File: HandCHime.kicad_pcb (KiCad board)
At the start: 4 copper layers, 38.1 x 22.6 mm, 18 parts, among them J1 USB_C_Receptacle_USB2.0, J2 Pins, SW0 BOOT, SW1 Row 0, Col 0, SW2 Row 0, Col 1, U1 CH552T, U2 USBLC6-2P6

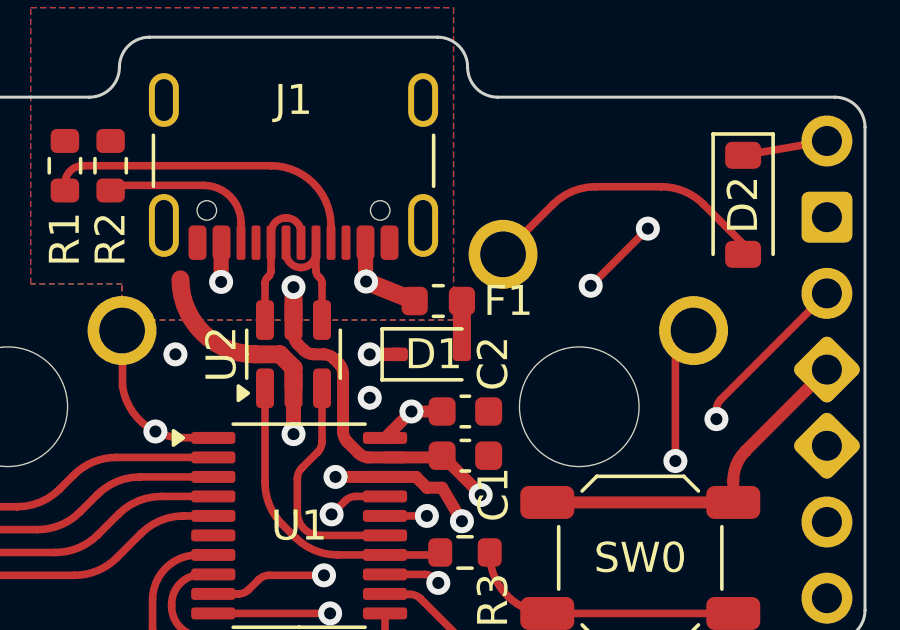
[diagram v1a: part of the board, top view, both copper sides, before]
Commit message: Move fuse away from newly lowered switch
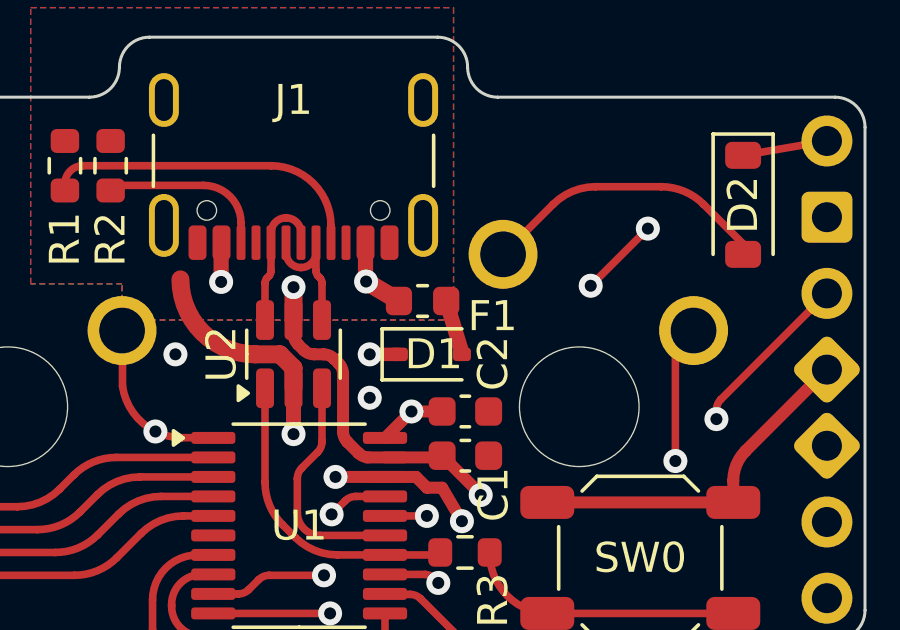
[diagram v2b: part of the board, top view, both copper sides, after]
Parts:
- moved F1 0.53 mm to (163.1, 46.5)
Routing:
- net Net-(D1-A): track 1.27 -> 1.80 mm
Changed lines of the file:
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@@
 	(footprint "Fuse:Fuse_0603_1608Metric"
 		(layer "F.Cu")
-		(at 163.576 46.482)
+		(at 163.051 46.482)
 		(descr "Fuse SMD 0603 (1608 Metric), square (rectangular) end terminal, IPC_7351 nominal, (Body size source: http://www.tortai-tech.com/upload/download/2011102023233369053.pdf), generated with kicad-footprint-generator")
 		(tags "fuse")
 		(property "Reference" "F1"
-			(at 2.3368 0 0)
+			(at 2.3368 0.508 0)
 			(layer "F.SilkS")
 			(effects
@@
 		(fp_arc
 			(start 6.497236 -6.998884)
-			(mid 6.850796 -6.85243)
+			(mid 6.85076 -6.852424)
 			(end 6.997236 -6.498884)
 			(stroke
@@
 		(fp_arc
 			(start 6.497236 -6.998884)
-			(mid 6.850796 -6.85243)
+			(mid 6.85076 -6.852424)
 			(end 6.997236 -6.498884)
 			(stroke
@@
 	)
 	(segment
-		(start 164.3635 48.1)
-		(end 164.3635 46.83)
-		(width 0.6)
+		(start 163.8385 46.482)
+		(end 164.3635 48.2)
+		(width 0.5)
 		(layer "F.Cu")
 		(net 3)
 	)
 	(segment
-		(start 156.337 45.847)
-		(end 156.337 44.805)
-		(width 0.508)
+		(start 161.168965 45.833058)
+		(end 162.2635 46.482)
+		(width 0.6)
 		(layer "F.Cu")
 		(net 4)
 	)
 	(segment
-		(start 161.15 45.814093)
-		(end 161.168965 45.833058)
+		(start 156.337 45.847)
+		(end 156.337 44.805)
 		(width 0.508)
 		(layer "F.Cu")
@@
 	)
 	(segment
-		(start 162.7885 46.482)
+		(start 161.15 45.814093)
 		(end 161.168965 45.833058)
-		(width 0.6)
+		(width 0.508)
 		(layer "F.Cu")
 		(net 4)

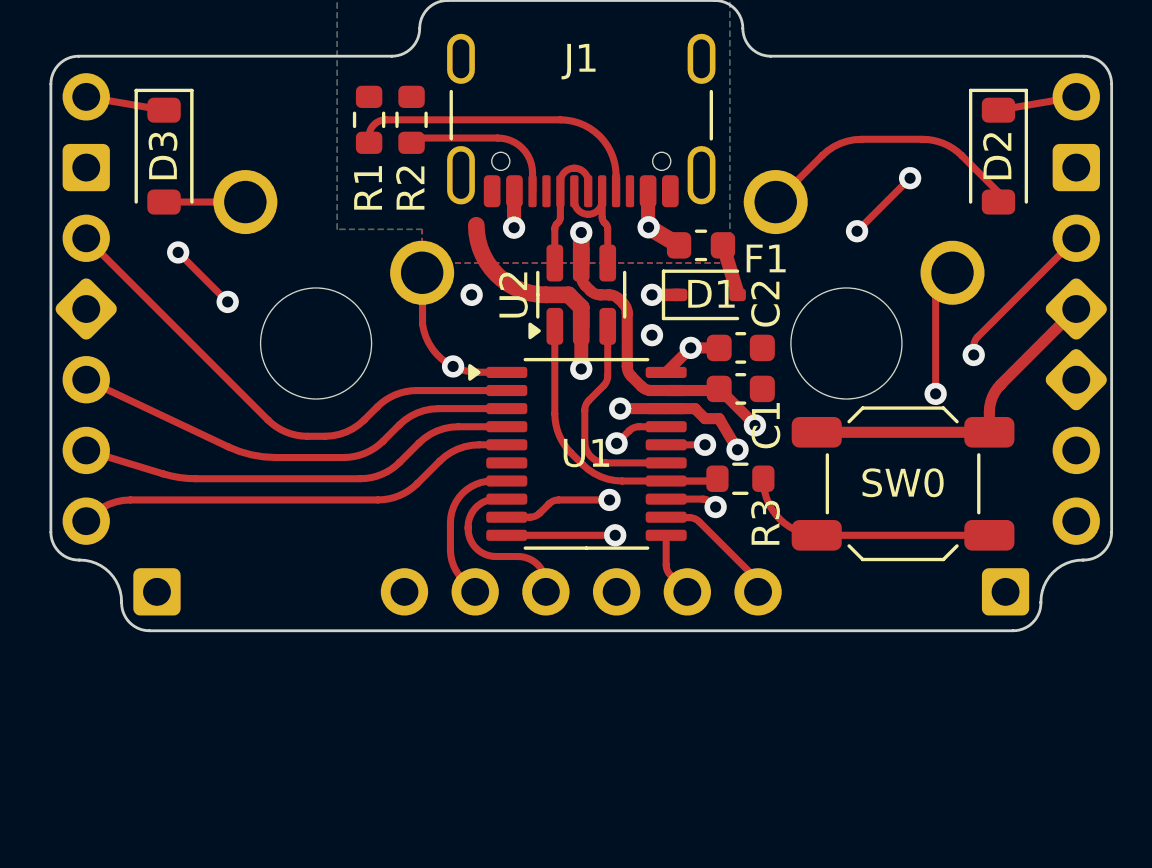
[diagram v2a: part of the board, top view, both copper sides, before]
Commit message: Reduce default via size
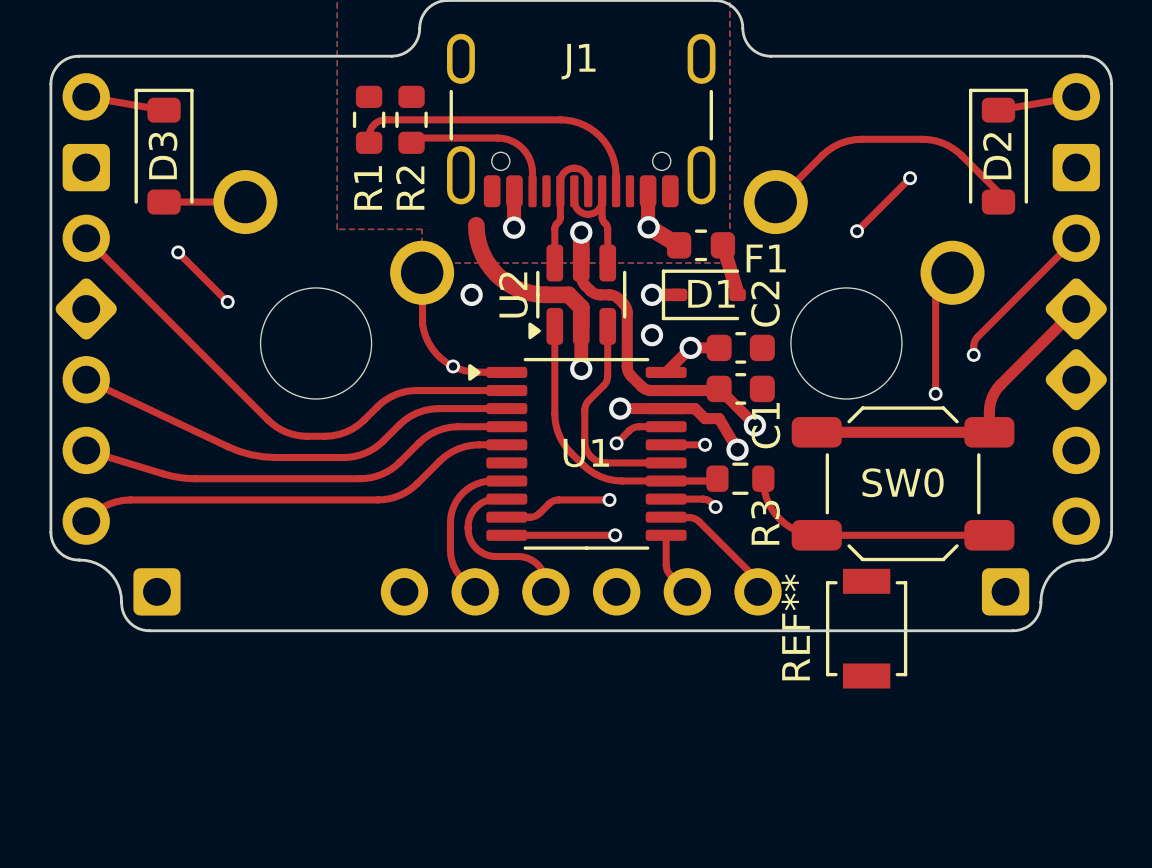
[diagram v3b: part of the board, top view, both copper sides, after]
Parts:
- added REF**: SW_SPST_B3U-1000P, Button_Switch_SMD:SW_SPST_B3U-1000P, F.Cu at (169.0, 60.2)

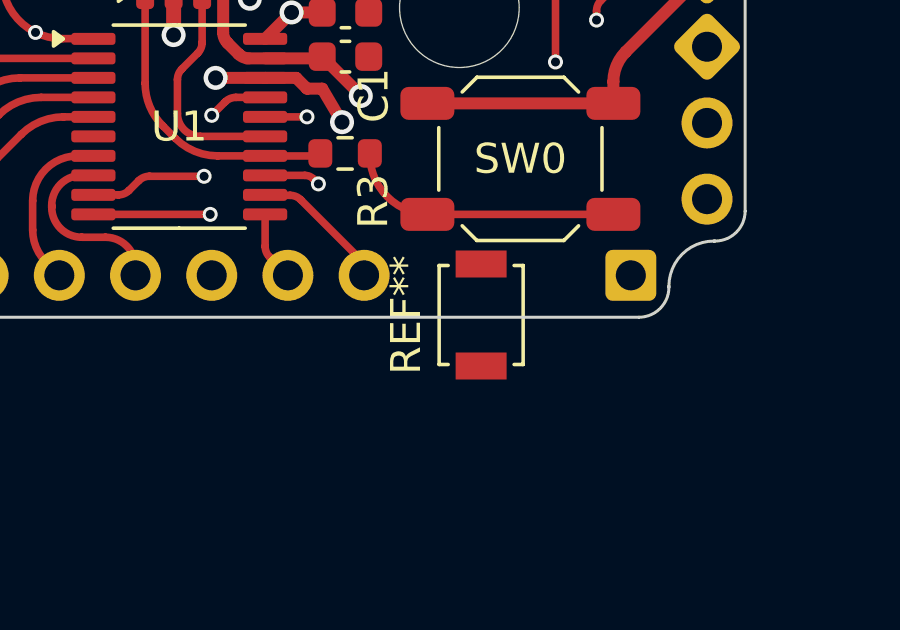
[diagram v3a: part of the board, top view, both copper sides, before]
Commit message: Remove erroneous button
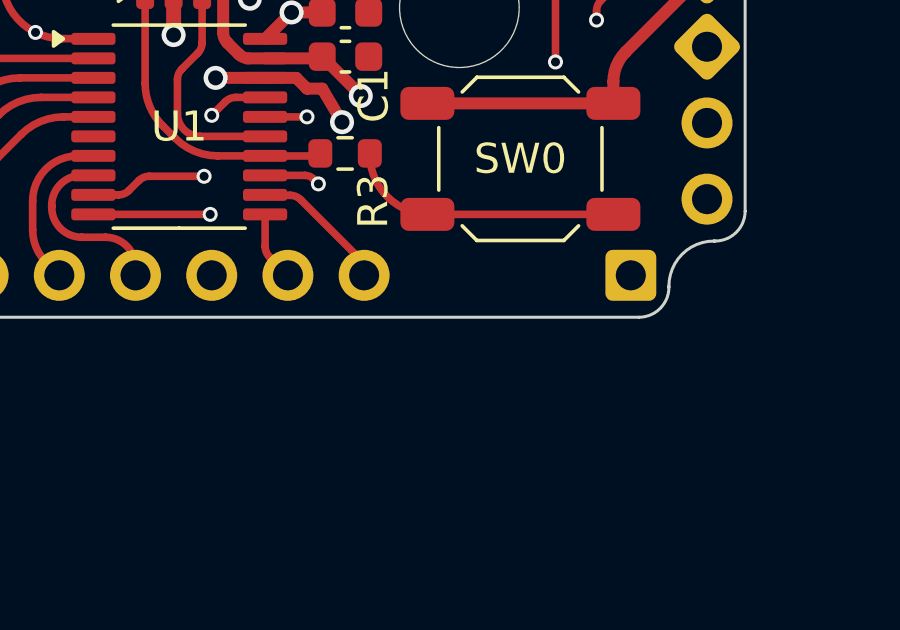
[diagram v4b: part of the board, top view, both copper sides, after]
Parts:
- removed REF**: SW_SPST_B3U-1000P, Button_Switch_SMD:SW_SPST_B3U-1000P
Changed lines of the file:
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@@
-		)
-	)
-	(footprint "Button_Switch_SMD:SW_SPST_B3U-1000P"
-		(layer "F.Cu")
-		(at 169 60.25 90)
-		(descr "Ultra-small-sized Tactile Switch with High Contact Reliability, Top-actuated Model, without Ground Terminal, without Boss")
-		(tags "Tactile Switch")
-		(property "Reference" "REF**"
-			(at 0 -2.5 90)
-			(layer "F.SilkS")
-			(effects
-				(font
-					(size 1 1)
-					(thickness 0.15)
-				)
-			)
-		)
-		(property "Value" "SW_SPST_B3U-1000P"
-			(at 0 2.5 90)
-			(layer "F.Fab")
-			(effects
-				(font
-					(size 1 1)
-					(thickness 0.15)
-				)
-			)
-		)
-		(property "Footprint" "Button_Switch_SMD:SW_SPST_B3U-1000P"
-			(at 0 0 90)
-			(unlocked yes)
-			(layer "F.Fab")
-			(hide yes)
-			(effects
-				(font
-					(size 1.27 1.27)
-					(thickness 0.15)
-				)
-			)
-		)
-		(property "Datasheet" ""
-			(at 0 0 90)
-			(unlocked yes)
-			(layer "F.Fab")
-			(hide yes)
-			(effects
-				(font
-					(size 1.27 1.27)
-					(thickness 0.15)
-				)
-			)
-		)
-		(property "Description" ""
-			(at 0 0 90)
-			(unlocked yes)
-			(layer "F.Fab")
-			(hide yes)
-			(effects
-				(font
-					(size 1.27 1.27)
-					(thickness 0.15)
-				)
-			)
-		)
-		(attr smd)
-		(fp_line
-			(start 1.65 -1.4)
-			(end 1.65 -1.1)
-			(stroke
-				(width 0.12)
-				(type solid)
-			)
-			(layer "F.SilkS")
-		)
-		(fp_line
-			(start -1.65 -1.4)
-			(end 1.65 -1.4)
-			(stroke
-				(width 0.12)
-				(type solid)
-			)
-			(layer "F.SilkS")
-		)
-		(fp_line
-			(start -1.65 -1.1)
-			(end -1.65 -1.4)
-			(stroke
-				(width 0.12)
-				(type solid)
-			)
-			(layer "F.SilkS")
-		)
-		(fp_line
-			(start -1.65 1.1)
-			(end -1.65 1.4)
-			(stroke
-				(width 0.12)
-				(type solid)
-			)
-			(layer "F.SilkS")
-		)
-		(fp_line
-			(start 1.65 1.4)
-			(end 1.65 1.1)
-			(stroke
-				(width 0.12)
-				(type solid)
-			)
-			(layer "F.SilkS")
-		)
-		(fp_line
-			(start -1.65 1.4)
-			(end 1.65 1.4)
-			(stroke
-				(width 0.12)
-				(type solid)
-			)
-			(layer "F.SilkS")
-		)
-		(fp_line
-			(start 2.4 -1.65)
-			(end -2.4 -1.65)
-			(stroke
-				(width 0.05)
-				(type solid)
-			)
-			(layer "F.CrtYd")
-		)
-		(fp_line
-			(start -2.4 -1.65)
-			(end -2.4 1.65)
-			(stroke
-				(width 0.05)
-				(type solid)
-			)
-			(layer "F.CrtYd")
-		)
-		(fp_line
-			(start 2.4 1.65)
-			(end 2.4 -1.65)
-			(stroke
-				(width 0.05)
-				(type solid)
-			)
-			(layer "F.CrtYd")
-		)
-		(fp_line
-			(start -2.4 1.65)
-			(end 2.4 1.65)
-			(stroke
-				(width 0.05)
-				(type solid)
-			)
-			(layer "F.CrtYd")
-		)
-		(fp_line
-			(start 1.5 -1.25)
-			(end 1.5 1.25)
-			(stroke
-				(width 0.1)
-				(type solid)
-			)
-			(layer "F.Fab")
-		)
-		(fp_line
-			(start -1.5 -1.25)
-			(end 1.5 -1.25)
-			(stroke
-				(width 0.1)
-				(type solid)
-			)
-			(layer "F.Fab")
-		)
-		(fp_line
-			(start 1.5 1.25)
-			(end -1.5 1.25)
-			(stroke
-				(width 0.1)
-				(type solid)
-			)
-			(layer "F.Fab")
-		)
-		(fp_line
-			(start -1.5 1.25)
-			(end -1.5 -1.25)
-			(stroke
-				(width 0.1)
-				(type solid)
-			)
-			(layer "F.Fab")
-		)
-		(fp_circle
-			(center 0 0)
-			(end 0.75 0)
-			(stroke
-				(width 0.1)
-				(type solid)
-			)
-			(fill none)
-			(layer "F.Fab")
-		)
-		(fp_text user "${REFERENCE}"
-			(at 0 -2.5 90)
-			(layer "F.Fab")
-			(effects
-				(font
-					(size 1 1)
-					(thickness 0.15)
-				)
-			)
-		)
-		(pad "1" smd rect
-			(at -1.700001 0 90)
-			(size 0.9 1.7)
-			(layers "F.Cu" "F.Paste" "F.Mask")
-		)
-		(pad "2" smd rect
-			(at 1.700001 0 90)
-			(size 0.9 1.7)
-			(layers "F.Cu" "F.Paste" "F.Mask")
-		)
-		(model "${KICAD8_3DMODEL_DIR}/Button_Switch_SMD.3dshapes/SW_SPST_B3U-1000P.wrl"
-			(offset
-				(xyz 0 0 0)
-			)
-			(scale
-				(xyz 1 1 1)
-			)
-			(rotate
-				(xyz 0 0 0)
-			)
 		)
 	)

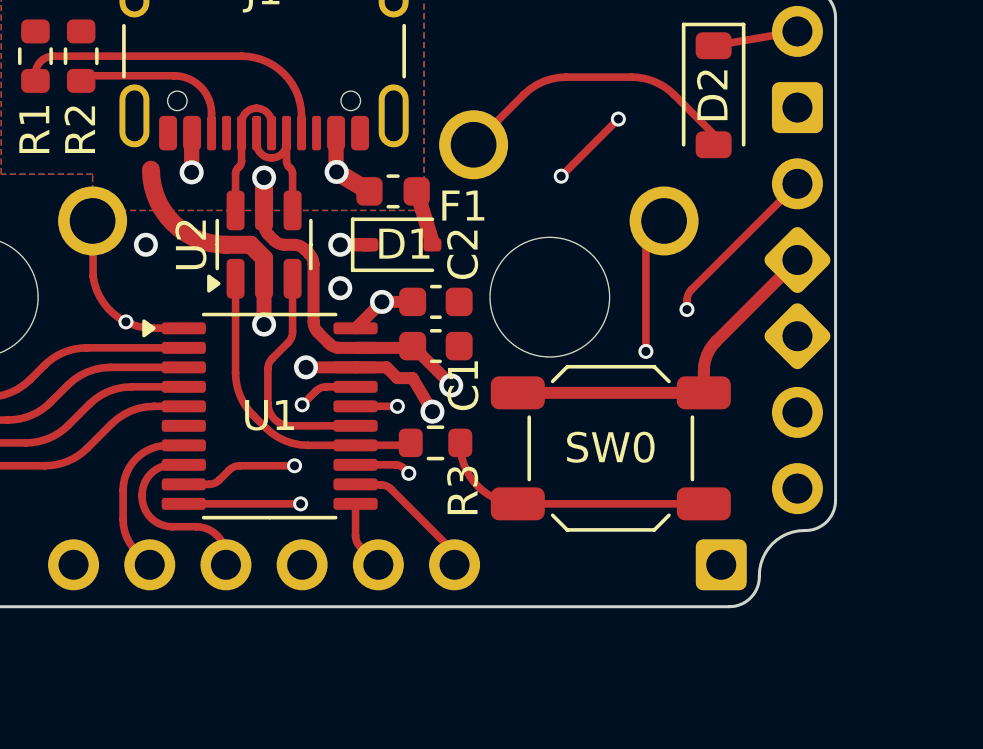
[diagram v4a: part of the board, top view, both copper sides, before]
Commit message: Update boot switch
 * Now uses the smaller B3U-1000P switch
 * Alternate pads provided on the keyswitch side so that Boot can be accessed by removing a keycap and poking through LED slot (on compatible switches)
 * Can now reroute C0 to avoid snaking around too much
 * Took advantage of now smaller vias on other traces
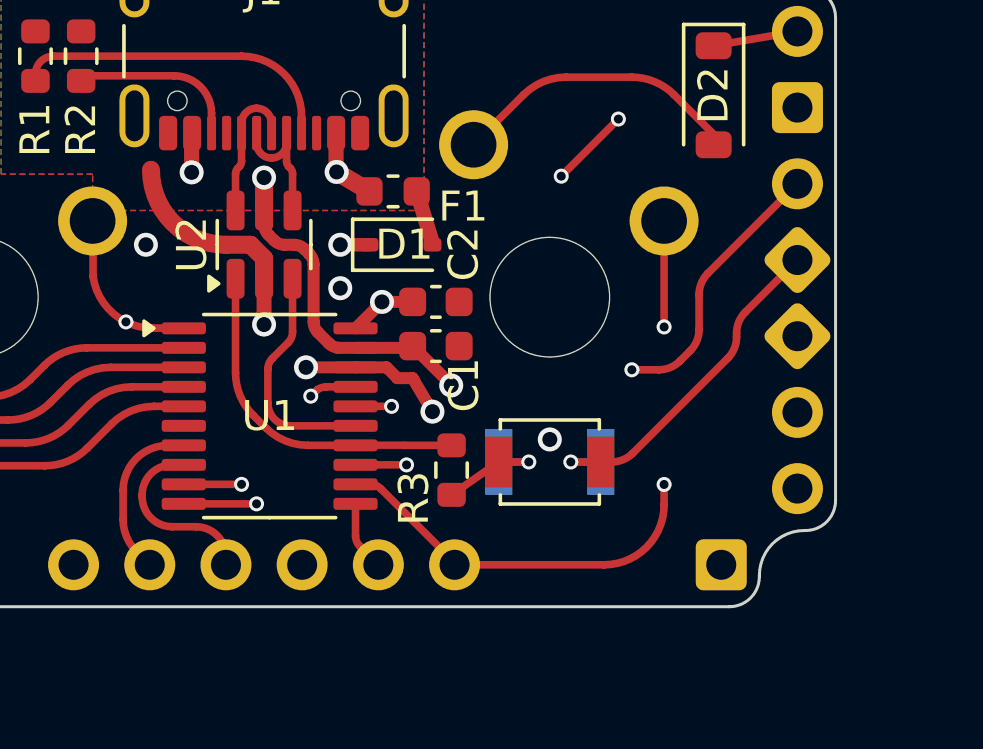
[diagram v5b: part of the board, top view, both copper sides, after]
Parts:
- R3: value 10k -> 5.1k
- SW0: footprint PCM_marbastlib-various:SW_SPST_SKQG_WithStem -> Project Library:SW_SPST_B3U-1000P
- moved SW0 2.08 mm to (168.3, 55.5), turned to 0 degrees
- moved R3 1.05 mm to (165.0, 55.8), turned to -90 degrees
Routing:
- net C0: track 32.8 -> 21.9 mm, vias 1 -> 2
- net Net-(R3-Pad2): track 9.50 -> 3.92 mm, vias 0 -> 1
- net BOOT: track 0.00 -> 1.56 mm
- net P12: track 9.72 -> 11.2 mm
- net P35: track 21.4 -> 20.0 mm
- net VCC: track 29.1 -> 28.1 mm
- net +3V3: track 55.8 -> 55.7 mm, vias 1 -> 2
- net GND: vias 5 -> 6
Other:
- board text removed: "BOOT"

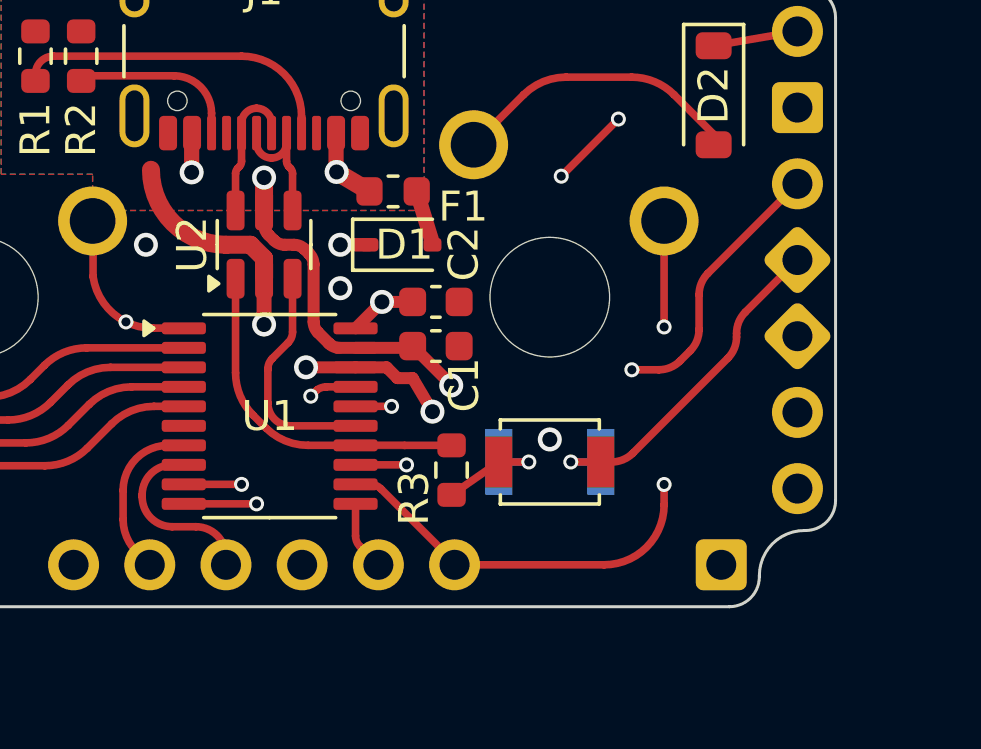
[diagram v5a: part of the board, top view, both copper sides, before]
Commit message: Swap +5 and 3.3V outputs
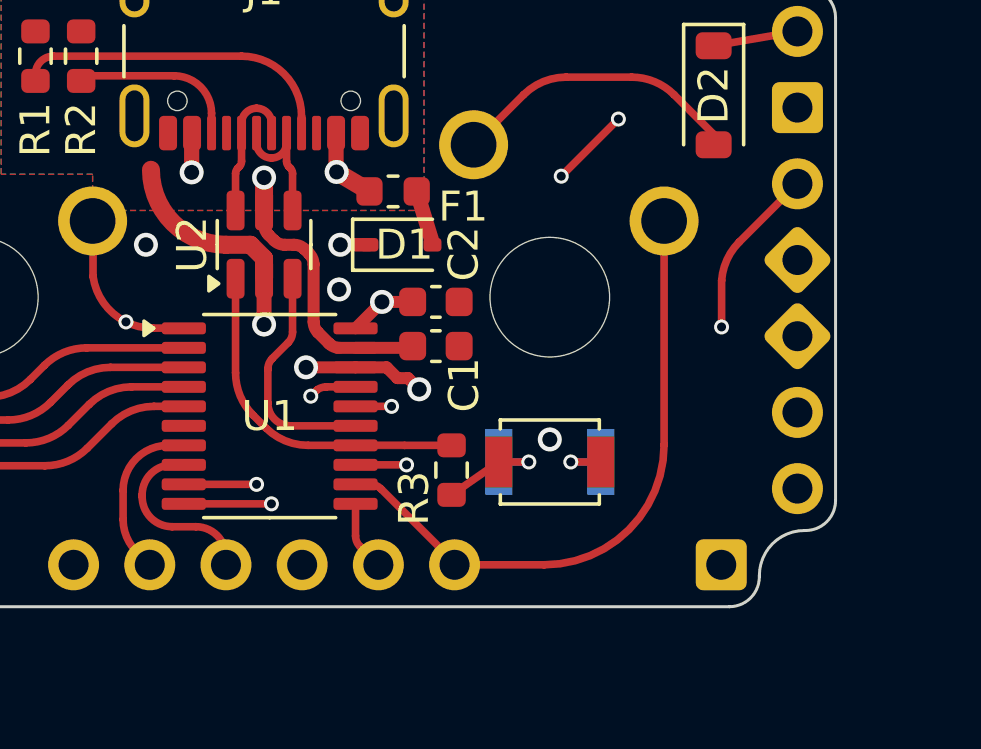
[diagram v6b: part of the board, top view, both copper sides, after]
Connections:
- J2 pad 18: VCC -> +3V3
- J2 pad 19: +3V3 -> VCC
- J2 pad 4: +3V3 -> VCC
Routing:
- net VCC: track 28.1 -> 53.8 mm, vias 3 -> 2
- net +3V3: track 55.7 -> 30.3 mm
- net C0: track 21.9 -> 21.0 mm, vias 2 -> 0
- net GND: track 7.01 -> 6.08 mm
- net RX: track 22.2 -> 21.7 mm
- net R0: track 59.0 -> 59.6 mm
